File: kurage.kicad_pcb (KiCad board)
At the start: 2 copper layers, 346 x 116.1 mm, 106 parts, among them SW1 ESC, SW10 R, SW11 Y, SW12 I, SW13 P, SW14 ], SW15 UNDEFINED2, SW16 CTRL, SW17 A, SW18 D, SW19 G, SW2 Q, SW20 J, SW21 L, SW22 ', SW23 S, SW24 F, SW25 H, SW26 K, SW27 ;, SW28 ENTER, SW29 UNDEFINED3, SW3 E, SW30 LSHIFT, SW31 Z, SW32 C, SW33 B, SW34 M, SW35 ., SW36 RSHIFT, SW37 X, SW38 V, SW39 N, SW4 T, SW40 ,, SW41 /, SW42 UP, SW43 LOWER, SW44 UNDEFINED1, SW45 WIN, SW46 RAISE, SW47 LEFT, SW48 RIGHT, SW49 LSPACE, SW5 U, SW50 RSPACE, SW51 ALT, SW52 DOWN, SW6 O, SW7 [, SW8 BACKSPACE, SW9 W, U1 Elite-C

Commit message: progress
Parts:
- SW1, SW44, SW46: footprint MX_Only:MXOnly-1U-Hotswap -> MX_Only:MXOnly-1.5U-Hotswap
- SW16, SW8: footprint MX_Only:MXOnly-1U-Hotswap -> MX_Only:MXOnly-1.75U-Hotswap
- SW28, SW30: footprint MX_Only:MXOnly-1U-Hotswap -> MX_Only:MXOnly-2.25U-Hotswap
- SW36, SW49: footprint MX_Only:MXOnly-1U-Hotswap -> MX_Only:MXOnly-2U-Hotswap
- SW43: footprint MX_Only:MXOnly-1U-Hotswap -> MX_Only:MXOnly-1.25U-Hotswap
- SW50: footprint MX_Only:MXOnly-1U-Hotswap -> MX_Only:MXOnly-2.75U-Hotswap
- moved SW51 188.1 mm to (224.2, 143.0), turned to 188 degrees
- moved SW50 187.9 mm to (176.7, 130.5), turned to 188 degrees
- moved SW11 187.8 mm to (147.9, 76.8), turned to 188 degrees
- moved SW12 187.8 mm to (185.6, 71.5), turned to 188 degrees
- moved SW13 187.8 mm to (223.3, 66.2), turned to 188 degrees
- moved SW20 187.8 mm to (178.8, 91.7), turned to 188 degrees
- moved SW21 187.8 mm to (216.6, 86.4), turned to 188 degrees
- moved SW25 187.8 mm to (160.0, 94.3), turned to 188 degrees
- moved SW26 187.8 mm to (197.7, 89.0), turned to 188 degrees
- moved SW34 187.8 mm to (186.2, 109.9), turned to 188 degrees
- moved SW35 187.8 mm to (223.9, 104.6), turned to 188 degrees
- moved SW39 187.8 mm to (167.3, 112.5), turned to 188 degrees
- moved SW40 187.8 mm to (205.1, 107.2), turned to 188 degrees
- moved SW5 187.8 mm to (166.7, 74.1), turned to 188 degrees
- moved SW6 187.8 mm to (204.5, 68.8), turned to 188 degrees
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
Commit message: fixing
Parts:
- moved D23 12.4 mm to (354.2, 141.1)
- moved D3 12.4 mm to (356.1, 81.6)
- moved D7 12.4 mm to (382.8, 144.8)
- moved D28 12.4 mm to (371.8, 111.4)
- moved D8 12.4 mm to (354.2, 132.3)
- moved SW35 12.4 mm to (211.7, 106.5)
- moved SW11 12.4 mm to (135.7, 78.7)
- moved SW13 12.4 mm to (211.1, 68.1)
- moved SW25 12.4 mm to (147.8, 96.3)
- moved SW27 12.4 mm to (227.2, 86.8)
- moved SW39 12.4 mm to (155.1, 114.5)
- moved SW41 12.4 mm to (236.7, 105.9)
- moved SW45 12.4 mm to (120.9, 136.5)
- moved SW49 12.4 mm to (92.6, 132.5)
- moved SW18 12.4 mm to (64.9, 90.2)
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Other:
- board size 346 x 116.1 mm -> 346.5 x 118.1 mm

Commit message: progress
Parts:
- D1, D10, D11, D12, D13, D14, D15, D16, D17, D18, D19, D2, D20, D21, D22, D23, D24, D25, D26, D27, D28, D29, D3, D30, D31, D32, D33, D34, D35, D36, D37, D38, D39, D4, D40, D41, D42, D43, D44, D45, D46, D47, D48, D49, D5, D50, D51, D52, D6, D7, D8, D9: moved to B.Cu
- moved D16 392.6 mm to (-9.65, 82.8), turned to 270 degrees
- moved D30 362.4 mm to (-16.7, 102.4), turned to 270 degrees
- moved D43 357.4 mm to (-16.7, 121.4), turned to 270 degrees
- moved D1 355.1 mm to (-9.40, 63.8), turned to 270 degrees
- moved D17 352.8 mm to (16.8, 82.5), turned to 270 degrees
- moved D2 350.8 mm to (14.5, 63.2), turned to 270 degrees
- moved D9 333.6 mm to (36.1, 63.8), turned to 262 degrees
- moved D23 321.3 mm to (38.4, 82.0), turned to 262 degrees
- moved D31 320.1 mm to (23.6, 102.4), turned to 270 degrees
- moved D10 315.8 mm to (74.2, 67.8), turned to 262 degrees
- moved D3 301.2 mm to (55.4, 65.0), turned to 262 degrees
- moved D37 297.8 mm to (45.2, 103.1), turned to 262 degrees
- moved D24 294.5 mm to (75.9, 87.6), turned to 262 degrees
- moved D18 290.5 mm to (57.4, 84.6), turned to 262 degrees
- moved D4 290.3 mm to (92.7, 70.9), turned to 262 degrees
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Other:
- outline, holes or cut-outs redrawn

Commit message: diodes
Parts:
- moved D15 1.54 mm to (299.9, 66.3)
- moved D2 1.23 mm to (14.7, 64.5)
- moved D3 1.22 mm to (55.2, 66.2)
- moved D11 1.21 mm to (127.0, 76.6)
- moved D18 1.18 mm to (57.2, 85.8)
- moved D10 1.07 mm to (74.0, 68.9)
- moved D23 1.06 mm to (38.4, 83.1)
- moved D8 1.01 mm to (269.0, 64.5)
- moved D7 0.97 mm to (223.7, 64.5)
- moved D17 0.96 mm to (16.8, 83.5)
- moved D27 0.95 mm to (218.9, 83.5)
- moved D28 0.89 mm to (259.9, 83.5)
- moved D5 0.89 mm to (145.9, 74.0)
- moved D24 0.79 mm to (76.1, 88.4)
- moved D46 0.78 mm to (195.9, 124.6)
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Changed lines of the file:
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@@
   )
   (module kbd:D3_TH (layer B.Cu)
-    (at 298.196 121.158 180)
+    (at 298.62272 121.412 180)
     (descr "Resitance 3 pas")
     (tags R)
@@
   )
   (module kbd:D3_TH (layer B.Cu)
-    (at 210.82 136.652 188)
+    (at 210.80476 136.78916 188)
     (descr "Resitance 3 pas")
     (tags R)
@@
   )
   (module kbd:D3_TH (layer B.Cu)
-    (at 146.558 131.572 278)
+    (at 146.878771 131.528528 278)
     (descr "Resitance 3 pas")
     (tags R)
@@
   )
   (module kbd:D3_TH (layer B.Cu)
-    (at 75.692 126.746 262)
+    (at 75.957077 126.859872 262)
     (descr "Resitance 3 pas")
     (tags R)
@@
   )
   (module kbd:D3_TH (layer B.Cu)
-    (at 317.5 121.158 180)
+    (at 317.67272 121.412 180)
     (descr "Resitance 3 pas")
     (tags R)
@@
   )
   (module kbd:D3_TH (layer B.Cu)
-    (at 279.654 121.158 180)
+    (at 279.57272 121.412 180)
     (descr "Resitance 3 pas")
     (tags R)
@@
   )
   (module kbd:D3_TH (layer B.Cu)
-    (at 195.58 123.952 278)
+    (at 195.945763 124.636203 278)
     (descr "Resitance 3 pas")
     (tags R)
@@
   )
   (module kbd:D3_TH (layer B.Cu)
-    (at 113.284 131.572 262)
+    (at 113.232409 132.100544 262)
     (descr "Resitance 3 pas")
     (tags R)
@@
   )
   (module kbd:D3_TH (layer B.Cu)
-    (at 51.816 123.19 262)
+    (at 51.929509 123.480294 262)
     (descr "Resitance 3 pas")
     (tags R)
@@
   )
   (module kbd:D3_TH (layer B.Cu)
-    (at -16.66875 121.412 270)
+    (at -16.79956 121.59488 270)
     (descr "Resitance 3 pas")
     (tags R)
@@
   )
   (module kbd:D3_TH (layer B.Cu)
-    (at 290.322 106.68 270)
+    (at 290.36772 107.315 270)
     (descr "Resitance 3 pas")
     (tags R)
@@
   )
   (module kbd:D3_TH (layer B.Cu)
-    (at 228.346 101.854 270)
+    (at 228.46919 102.55123 270)
     (descr "Resitance 3 pas")
     (tags R)
@@
   )
   (module kbd:D3_TH (layer B.Cu)
-    (at 184.15 106.68 278)
+    (at 184.228128 107.047087 278)
     (descr "Resitance 3 pas")
     (tags R)
@@
   )
   (module kbd:D3_TH (layer B.Cu)
-    (at 146.558 112.014 278)
+    (at 146.498915 112.349582 278)
     (descr "Resitance 3 pas")
     (tags R)
@@
   )
   (module kbd:D3_TH (layer B.Cu)
-    (at 82.804 108.458 262)
+    (at 82.874389 108.592558 262)
     (descr "Resitance 3 pas")
     (tags R)
@@
   )
   (module kbd:D3_TH (layer B.Cu)
-    (at 45.212 103.124 262)
+    (at 45.145176 103.290063 262)
     (descr "Resitance 3 pas")
     (tags R)
@@
   )
   (module kbd:D3_TH (layer B.Cu)
-    (at 247.65 101.854 270)
+    (at 247.97893 102.55123 270)
     (descr "Resitance 3 pas")
     (tags R)
@@
   )
   (module kbd:D3_TH (layer B.Cu)
-    (at 202.946 103.886 278)
+    (at 203.092735 104.39584 278)
     (descr "Resitance 3 pas")
     (tags R)
@@
   )
   (module kbd:D3_TH (layer B.Cu)
-    (at 165.263519 109.396804 278)
+    (at 165.363521 109.698335 278)
     (descr "Resitance 3 pas")
     (tags R)
@@
   )
   (module kbd:D3_TH (layer B.Cu)
-    (at 101.854 110.998 262)
+    (at 101.738996 111.243806 262)
     (descr "Resitance 3 pas")
     (tags R)
@@
   )
   (module kbd:D3_TH (layer B.Cu)
-    (at 64.008 105.918 262)
+    (at 64.009782 105.941311 262)
     (descr "Resitance 3 pas")
     (tags R)
@@
   )
   (module kbd:D3_TH (layer B.Cu)
-    (at 23.622 102.39375 270)
+    (at 23.68169 102.55123 270)
     (descr "Resitance 3 pas")
     (tags R)
@@
   )
   (module kbd:D3_TH (layer B.Cu)
-    (at -16.66875 102.39375 270)
+    (at -16.33982 102.55123 270)
     (descr "Resitance 3 pas")
     (tags R)
@@
   )
   (module kbd:D3_TH (layer B.Cu)
-    (at 304.546 77.978 270)
+    (at 304.65649 78.73873 270)
     (descr "Resitance 3 pas")
     (tags R)
@@
   )
   (module kbd:D3_TH (layer B.Cu)
-    (at 259.334 82.804 270)
+    (at 259.88518 83.50123 270)
     (descr "Resitance 3 pas")
     (tags R)
@@
   )
   (module kbd:D3_TH (layer B.Cu)
-    (at 218.948 82.55 270)
+    (at 218.94419 83.50123 270)
     (descr "Resitance 3 pas")
     (tags R)
@@
   )
   (module kbd:D3_TH (layer B.Cu)
-    (at 176.784 88.392 278)
+    (at 176.860729 88.845293 278)
     (descr "Resitance 3 pas")
     (tags R)
@@
   )
   (module kbd:D3_TH (layer B.Cu)
-    (at 138.938 93.472 278)
+    (at 139.131515 94.147788 278)
     (descr "Resitance 3 pas")
     (tags R)
@@
   )
   (module kbd:D3_TH (layer B.Cu)
-    (at 75.946 87.63 262)
+    (at 76.093333 88.402328 262)
     (descr "Resitance 3 pas")
     (tags R)
@@
   )
   (module kbd:D3_TH (layer B.Cu)
-    (at 38.354 82.042 262)
+    (at 38.36412 83.099833 262)
     (descr "Resitance 3 pas")
     (tags R)
@@
   )
   (module kbd:D3_TH (layer B.Cu)
-    (at 237.998 82.804 270)
+    (at 237.99419 83.50123 270)
     (descr "Resitance 3 pas")
     (tags R)
@@
   )
   (module kbd:D3_TH (layer B.Cu)
-    (at 195.58 85.852 278)
+    (at 195.725335 86.194045 278)
     (descr "Resitance 3 pas")
     (tags R)
@@
   )
   (module kbd:D3_TH (layer B.Cu)
-    (at 157.734 90.932 278)
+    (at 157.996122 91.49654 278)
     (descr "Resitance 3 pas")
     (tags R)
@@
   )
   (module kbd:D3_TH (layer B.Cu)
-    (at 94.996 90.424 262)
+    (at 94.95794 91.053576 262)
     (descr "Resitance 3 pas")
     (tags R)
@@
   )
   (module kbd:D3_TH (layer B.Cu)
-    (at 57.404 84.582 262)
+    (at 57.228727 85.75108 262)
     (descr "Resitance 3 pas")
     (tags R)
@@
   )
   (module kbd:D3_TH (layer B.Cu)
-    (at 16.764 82.55 270)
+    (at 16.83639 83.50758 270)
     (descr "Resitance 3 pas")
     (tags R)
@@
   )
   (module kbd:D3_TH (layer B.Cu)
-    (at -9.652 82.804 270)
+    (at -9.35736 83.50758 270)
     (descr "Resitance 3 pas")
     (tags R)
@@
   )
   (module kbd:D3_TH (layer B.Cu)
-    (at 299.72 67.818 270)
+    (at 299.89399 66.29273 270)
     (descr "Resitance 3 pas")
     (tags R)
@@
   )
   (module kbd:D3_TH (layer B.Cu)
-    (at 242.57 63.754 270)
+    (at 242.75669 64.45123 270)
     (descr "Resitance 3 pas")
     (tags R)
@@
   )
   (module kbd:D3_TH (layer B.Cu)
-    (at 202.438 65.786 278)
+    (at 202.506391 66.003814 278)
     (descr "Resitance 3 pas")
     (tags R)
@@
   )
   (module kbd:D3_TH (layer B.Cu)
-    (at 164.592 70.612 278)
+    (at 164.777178 71.30631 278)
     (descr "Resitance 3 pas")
     (tags R)
@@
   )
   (module kbd:D3_TH (layer B.Cu)
-    (at 126.746 75.438 278)
+    (at 127.047964 76.608805 278)
     (descr "Resitance 3 pas")
     (tags R)
@@
   )
   (module kbd:D3_TH (layer B.Cu)
-    (at 74.168 67.818 262)
+    (at 74.028429 68.874909 262)
     (descr "Resitance 3 pas")
     (tags R)
@@
   )
   (module kbd:D3_TH (layer B.Cu)
-    (at 36.068 63.754 262)
+    (at 36.299216 63.572414 262)
     (descr "Resitance 3 pas")
     (tags R)
@@
   )
   (module kbd:D3_TH (layer B.Cu)
-    (at 268.224 63.754 270)
+    (at 268.95044 64.45123 270)
     (descr "Resitance 3 pas")
     (tags R)
@@
   )
   (module kbd:D3_TH (layer B.Cu)
-    (at 223.52 63.5 270)
+    (at 223.70669 64.45123 270)
     (descr "Resitance 3 pas")
     (tags R)
@@
   )
   (module kbd:D3_TH (layer B.Cu)
-    (at 183.642 68.326 278)
+    (at 183.641785 68.655062 278)
     (descr "Resitance 3 pas")
     (tags R)
@@
   )
   (module kbd:D3_TH (layer B.Cu)
-    (at 145.542 73.152 278)
+    (at 145.912571 73.957557 278)
     (descr "Resitance 3 pas")
     (tags R)
@@
   )
   (module kbd:D3_TH (layer B.Cu)
-    (at 92.71 70.866 262)
+    (at 92.893036 71.526157 262)
     (descr "Resitance 3 pas")
     (tags R)
@@
   )
   (module kbd:D3_TH (layer B.Cu)
-    (at 55.372 65.024 262)
+    (at 55.163823 66.223662 262)
     (descr "Resitance 3 pas")
     (tags R)
@@
   )
   (module kbd:D3_TH (layer B.Cu)
-    (at 14.478 63.246 270)
+    (at 14.73454 64.45123 270)
     (descr "Resitance 3 pas")
     (tags R)
@@
   )
   (module kbd:D3_TH (layer B.Cu)
-    (at -9.398 63.754 270)
-    (descr "Resitance 3 pas")
-    (tags R)
+    (at -9.07796 64.45123 270)
+    (descr "Resitance 3 pas")
+    (tags R)

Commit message: progress
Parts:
- moved SW18 4.83 mm to (69.7, 89.7)
- moved SW21 4.83 mm to (209.2, 87.8)
- moved SW36 4.83 mm to (270.1, 105.3)
- moved SW41 4.83 mm to (241.5, 105.3)
- moved D1 4.83 mm to (-4.27, 63.9)
- moved SW2 4.83 mm to (27.8, 67.2)
- moved D11 4.83 mm to (131.9, 76.1)
- moved SW32 4.83 mm to (76.5, 109.8)
- moved D33 4.83 mm to (106.5, 110.7)
- moved SW6 4.83 mm to (197.1, 70.3)
- moved SW27 4.83 mm to (232.0, 86.3)
- moved D3 4.83 mm to (60.0, 65.7)
- moved D49 4.83 mm to (80.8, 126.3)
- moved SW35 4.83 mm to (216.5, 106.0)
- moved SW31 4.83 mm to (36.7, 105.3)
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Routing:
- net COL3: track 0.00 -> 500.3 mm
- net COL2: track 0.00 -> 277.3 mm
- net COL6: track 0.00 -> 201.7 mm
- net COL4: track 0.00 -> 161.0 mm
- net COL5: track 0.00 -> 151.9 mm
- net COL1: track 0.00 -> 150.8 mm
- net COL7: track 0.00 -> 108.9 mm
- net COL0: track 0.00 -> 62.1 mm
- net Net-(D48-Pad2): track 0.00 -> 17.1 mm
- net Net-(D52-Pad2): track 0.00 -> 16.7 mm
- net Net-(D47-Pad2): track 0.00 -> 16.5 mm
- net Net-(D51-Pad2): track 0.00 -> 15.3 mm
- net Net-(D36-Pad2): track 0.00 -> 14.9 mm
- net Net-(D30-Pad2): track 0.00 -> 14.9 mm
- net Net-(D28-Pad2): track 0.00 -> 14.9 mm
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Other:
- net class Default: trace_width 0.25 -> 0.254
- net class Power added: clearance 0.2, trace_width 0.381, via_dia 0.8, via_drill 0.4

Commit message: progress 2
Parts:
- moved SW36 1.99 mm to (272.1, 105.0)
- moved D51 1.99 mm to (217.6, 135.9)
- moved SW25 1.99 mm to (154.5, 95.4)
- moved D15 1.99 mm to (306.7, 65.4)
- moved D52 1.99 mm to (305.4, 120.6)
- moved SW10 1.99 mm to (88.5, 72.4)
- moved SW24 1.99 mm to (90.6, 92.0)
- moved SW46 1.99 mm to (211.3, 125.9)
- moved OL1 1.99 mm to (25.4, 46.6)
- moved SW1 1.99 mm to (5.94, 66.9)
- moved D49 1.99 mm to (82.7, 126.0)
- moved SW50 1.99 mm to (171.3, 131.5)
- moved SW8 1.99 mm to (284.0, 66.9)
- moved D21 1.99 mm to (202.5, 85.3)
- moved D28 1.99 mm to (266.7, 82.6)
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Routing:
- net ROW6: track 3.67 -> 371.0 mm
- net ROW0: track 4.90 -> 300.6 mm
- net ROW3: track 3.67 -> 287.0 mm
- net ROW1: track 2.45 -> 285.5 mm
- net ROW4: track 3.67 -> 283.3 mm
- net ROW2: track 3.68 -> 266.2 mm
- net ROW7: track 1.22 -> 262.7 mm
- net ROW5: track 2.45 -> 260.8 mm
- net COL4: track 161.0 -> 264.4 mm
- net GND: track 0.00 -> 36.1 mm
- net +5V: track 0.00 -> 35.0 mm
- net Net-(D35-Pad2): track 6.38 -> 7.60 mm
- net Net-(D24-Pad2): track 6.38 -> 7.60 mm
- net Net-(D33-Pad2): track 6.38 -> 7.60 mm
- net Net-(D50-Pad2): track 13.7 -> 14.9 mm
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
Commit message: save
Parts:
- SW10, SW11, SW12, SW13, SW14, SW15, SW17, SW18, SW19, SW2, SW20, SW21, SW22, SW23, SW24, SW25, SW26, SW27, SW29, SW3, SW31, SW32, SW33, SW34, SW35, SW37, SW38, SW39, SW4, SW40, SW41, SW42, SW45, SW47, SW48, SW5, SW51, SW52, SW6, SW7, SW9: footprint MX_Only:MXOnly-1U-Hotswap -> kbd:CherryMX_Hotswap
- U1: value Elite-C -> ProMicro; footprint Keebio-Parts:Elite-C -> kbd:ProMicro_v3; moved to B.Cu
- moved D9 3.37 mm to (42.5, 66.0)
- moved U1 0.50 mm to (6.78, 46.6), turned to 270 degrees
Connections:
- U1 pad 1: Net-(U1-Pad1) -> ROW0
- U1 pad 10: Net-(U1-Pad10) -> ROW4
- U1 pad 11: Net-(U1-Pad11) -> ROW7
- U1 pad 12: Net-(U1-Pad12) -> ROW6
- U1 pad 13: Net-(U1-Pad13) -> COL7
- U1 pad 14: Net-(U1-Pad14) -> COL6
- U1 pad 15: Net-(U1-Pad15) -> COL5
- U1 pad 16: Net-(U1-Pad16) -> COL4
- U1 pad 17: Net-(U1-Pad17) -> COL3
- U1 pad 18: Net-(U1-Pad18) -> COL2
- U1 pad 19: Net-(U1-Pad19) -> COL1
- U1 pad 2: Net-(U1-Pad2) -> ROW1
- U1 pad 20: Net-(U1-Pad20) -> COL0
- U1 pad 21: Net-(U1-Pad21) -> +5V
- U1 pad 22: +5V -> Net-(U1-Pad22)
- U1 pad 7: Net-(U1-Pad7) -> ROW3
- U1 pad 8: Net-(U1-Pad8) -> ROW2
- U1 pad 9: Net-(U1-Pad9) -> ROW5
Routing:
- net COL7: track 108.9 -> 424.9 mm
- net COL6: track 201.7 -> 459.8 mm
- net COL5: track 151.9 -> 373.7 mm
- net ROW7: track 262.7 -> 451.5 mm, vias 0 -> 2
- net COL4: track 264.4 -> 449.4 mm
- net COL3: track 500.3 -> 647.5 mm
- net ROW5: track 260.8 -> 381.7 mm
- net ROW6: track 371.0 -> 469.8 mm
- net COL2: track 277.3 -> 367.1 mm
- net ROW3: track 287.0 -> 374.0 mm
- net ROW4: track 283.3 -> 356.0 mm
- net ROW1: track 285.5 -> 338.1 mm
- net ROW2: track 266.2 -> 315.4 mm
- net COL0: track 62.1 -> 107.0 mm
- net COL1: track 150.8 -> 193.6 mm
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
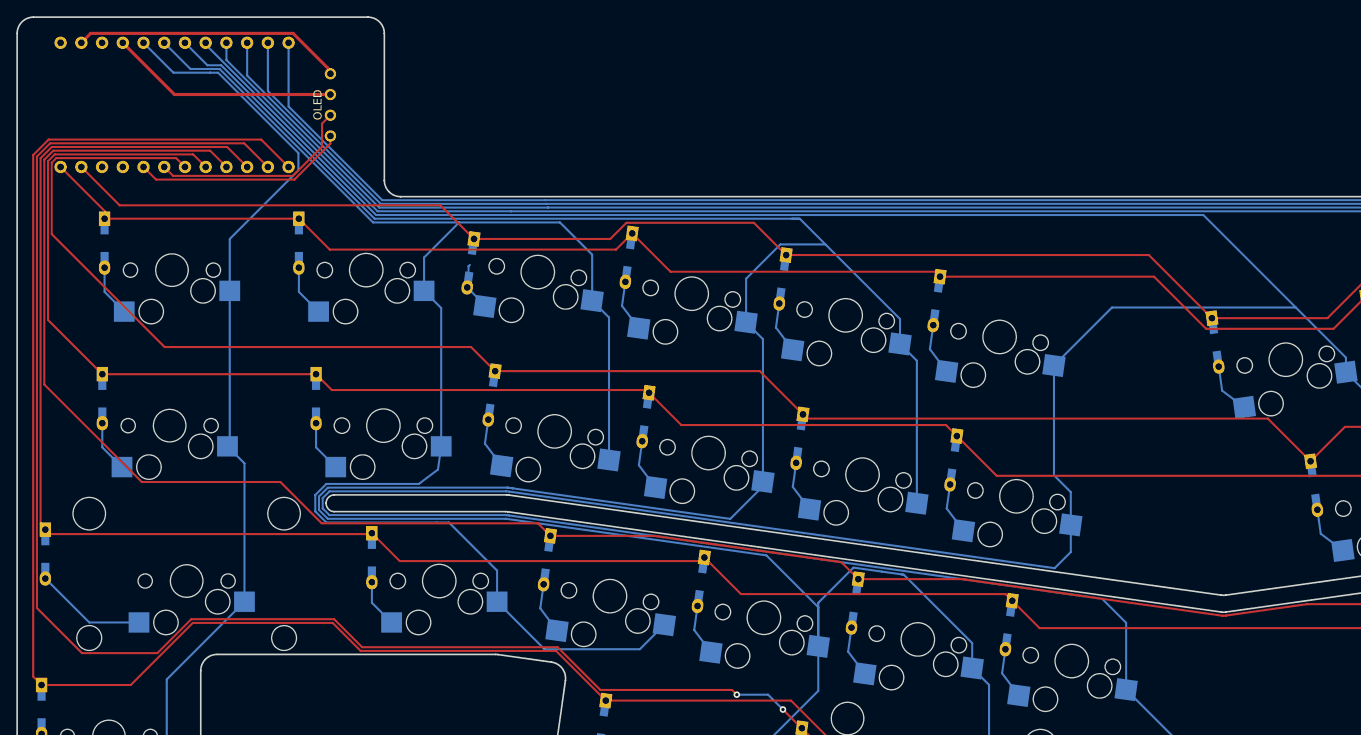
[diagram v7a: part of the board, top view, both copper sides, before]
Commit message: flip pro micro
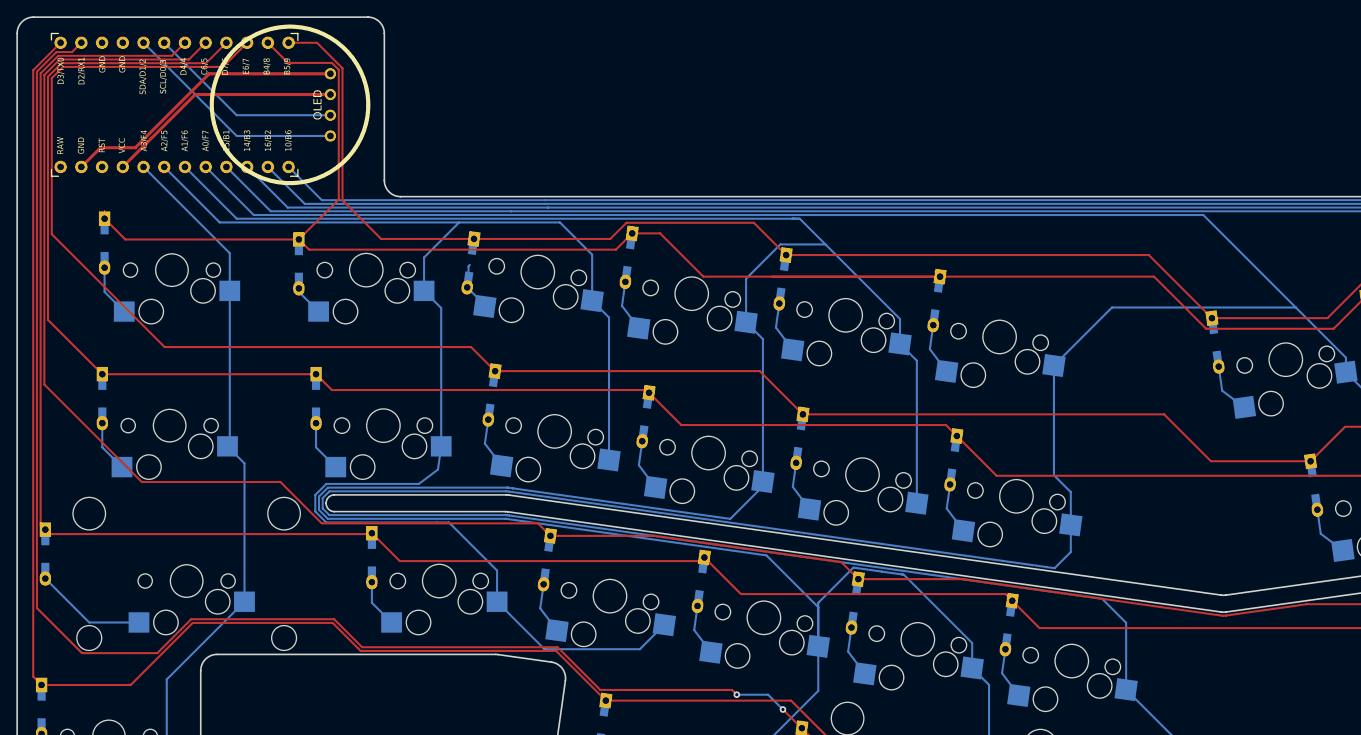
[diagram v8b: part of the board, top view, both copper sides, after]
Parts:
- U1: moved to F.Cu
- moved D2 2.54 mm to (21.5, 66.1)
- turned U1 to 90 degrees
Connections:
- U1 pad 1: ROW0 -> ROW6
- U1 pad 10: ROW4 -> ROW3
- U1 pad 11: ROW7 -> ROW0
- U1 pad 12: ROW6 -> ROW1
- U1 pad 2: ROW1 -> ROW7
- U1 pad 3: GND -> Net-(U1-Pad3)
- U1 pad 4: GND -> Net-(U1-Pad4)
- U1 pad 7: ROW3 -> ROW4
- U1 pad 8: ROW2 -> ROW5
- U1 pad 9: ROW5 -> ROW2
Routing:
- net ROW0: track 311.0 -> 357.7 mm
- net COL0: track 107.0 -> 81.6 mm
- net ROW3: track 374.0 -> 393.8 mm
- net ROW6: track 469.8 -> 451.5 mm
- net ROW2: track 315.4 -> 329.0 mm
- net ROW7: track 451.5 -> 438.6 mm
- net COL7: track 424.9 -> 414.0 mm
- net COL6: track 459.8 -> 450.1 mm
- net ROW1: track 338.1 -> 328.5 mm
- net COL5: track 373.7 -> 365.0 mm
- net ROW5: track 381.7 -> 390.1 mm
- net COL4: track 449.4 -> 441.9 mm
- net COL3: track 647.5 -> 641.1 mm
- net COL1: track 193.6 -> 187.3 mm
- net COL2: track 367.1 -> 361.0 mm
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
